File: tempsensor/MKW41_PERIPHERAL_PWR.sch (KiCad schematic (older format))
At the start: 39 parts, among them J3 Conn_ARM_JTAG_SWD_10, J4 USB_B_Micro, Q1 BSS806N, Q2 BSS806N, SW3 ~RST, SW4 ~INT, U6 BQ24012

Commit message: Added footprints to tempsensor.
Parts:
- C16, C25, C26: footprint (none) -> Capacitor_SMD:C_0603_1608Metric
- C17, C18, C19, C20, C22, C23, C24, C27, C28, C29, C30, C31, C32: footprint (none) -> Capacitor_SMD:C_0402_1005Metric
- J3: footprint (none) -> Connector_PinHeader_1.27mm:PinHeader_2x05_P1.27mm_Vertical_SMD
- L3, L4: footprint (none) -> Inductor_SMD:L_0402_1005Metric
- SW3: footprint Button_Switch_THT:SW_PUSH_6mm_H5mm -> Button_Switch_SMD:SW_SPST_Panasonic_EVQPL_3PL_5PL_PT_A08
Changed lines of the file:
@@
 F 0 "SW3" V 2504 1498 50  0000 L CNN
 F 1 "~RST" V 2595 1498 50  0000 L CNN
-F 2 "Button_Switch_THT:SW_PUSH_6mm_H5mm" H 2550 1550 50  0001 C CNN
+F 2 "Button_Switch_SMD:SW_SPST_Panasonic_EVQPL_3PL_5PL_PT_A08" H 2550 1550 50  0001 C CNN
 F 3 "~" H 2550 1550 50  0001 C CNN
 	1    2550 1350
@@
 F 0 "J3" H 700 1950 50  0000 R CNN
 F 1 "Conn_ARM_JTAG_SWD_10" H 1950 1950 50  0000 R CNN
-F 2 "" H 1000 1400 50  0001 C CNN
+F 2 "Connector_PinHeader_1.27mm:PinHeader_2x05_P1.27mm_Vertical_SMD" H 1000 1400 50  0001 C CNN
 F 3 "http://infocenter.arm.com/help/topic/com.arm.doc.ddi0314h/DDI0314H_coresight_components_trm.pdf" V 650 150 50  0001 C CNN
 	1    1000 1400
@@
 F 0 "C22" H 3565 1646 50  0000 L CNN
 F 1 "10n" H 3565 1555 50  0000 L CNN
-F 2 "" H 3488 1450 50  0001 C CNN
+F 2 "Capacitor_SMD:C_0402_1005Metric" H 3488 1450 50  0001 C CNN
 F 3 "~" H 3450 1600 50  0001 C CNN
 	1    3450 1600
@@
 F 0 "C16" H 9065 1046 50  0000 L CNN
 F 1 "10u" H 9065 955 50  0000 L CNN
-F 2 "" H 8988 850 50  0001 C CNN
+F 2 "Capacitor_SMD:C_0603_1608Metric" H 8988 850 50  0001 C CNN
 F 3 "~" H 8950 1000 50  0001 C CNN
 	1    8950 1000
@@
 F 0 "C18" H 9965 1046 50  0000 L CNN
 F 1 "1u" H 9965 955 50  0000 L CNN
-F 2 "" H 9888 850 50  0001 C CNN
+F 2 "Capacitor_SMD:C_0402_1005Metric" H 9888 850 50  0001 C CNN
 F 3 "~" H 9850 1000 50  0001 C CNN
 	1    9850 1000
@@
 F 0 "C19" H 10365 1046 50  0000 L CNN
 F 1 "100n" H 10365 955 50  0000 L CNN
-F 2 "" H 10288 850 50  0001 C CNN
+F 2 "Capacitor_SMD:C_0402_1005Metric" H 10288 850 50  0001 C CNN
 F 3 "~" H 10250 1000 50  0001 C CNN
 	1    10250 1000
@@
 F 0 "C20" H 10865 1046 50  0000 L CNN
 F 1 "100n" H 10865 955 50  0000 L CNN
-F 2 "" H 10788 850 50  0001 C CNN
+F 2 "Capacitor_SMD:C_0402_1005Metric" H 10788 850 50  0001 C CNN
 F 3 "~" H 10750 1000 50  0001 C CNN
 	1    10750 1000
@@
 F 0 "L3" V 10740 1750 50  0000 C CNN
 F 1 "100n" V 10649 1750 50  0000 C CNN
-F 2 "" H 10550 1750 50  0001 C CNN
+F 2 "Inductor_SMD:L_0402_1005Metric" H 10550 1750 50  0001 C CNN
 F 3 "~" H 10550 1750 50  0001 C CNN
 	1    10550 1750
@@
 F 0 "C23" H 10865 1996 50  0000 L CNN
 F 1 "1u" H 10865 1905 50  0000 L CNN
-F 2 "" H 10788 1800 50  0001 C CNN
+F 2 "Capacitor_SMD:C_0402_1005Metric" H 10788 1800 50  0001 C CNN
 F 3 "~" H 10750 1950 50  0001 C CNN
 	1    10750 1950
@@
 F 0 "C24" H 10865 2846 50  0000 L CNN
 F 1 "100n" H 10865 2755 50  0000 L CNN
-F 2 "" H 10788 2650 50  0001 C CNN
+F 2 "Capacitor_SMD:C_0402_1005Metric" H 10788 2650 50  0001 C CNN
 F 3 "~" H 10750 2800 50  0001 C CNN
 	1    10750 2800
@@
 F 0 "C26" H 8915 3746 50  0000 L CNN
 F 1 "10u" H 8915 3655 50  0000 L CNN
-F 2 "" H 8838 3550 50  0001 C CNN
+F 2 "Capacitor_SMD:C_0603_1608Metric" H 8838 3550 50  0001 C CNN
 F 3 "~" H 8800 3700 50  0001 C CNN
 	1    8800 3700
@@
 F 0 "L4" V 9190 3500 50  0000 C CNN
 F 1 "100n" V 9099 3500 50  0000 C CNN
-F 2 "" H 9000 3500 50  0001 C CNN
+F 2 "Inductor_SMD:L_0402_1005Metric" H 9000 3500 50  0001 C CNN
 F 3 "~" H 9000 3500 50  0001 C CNN
 	1    9000 3500
@@
 F 0 "C27" H 9315 3746 50  0000 L CNN
 F 1 "1u" H 9315 3655 50  0000 L CNN
-F 2 "" H 9238 3550 50  0001 C CNN
+F 2 "Capacitor_SMD:C_0402_1005Metric" H 9238 3550 50  0001 C CNN
 F 3 "~" H 9200 3700 50  0001 C CNN
 	1    9200 3700
@@
 F 0 "C28" H 9665 3746 50  0000 L CNN
 F 1 "1u" H 9665 3655 50  0000 L CNN
-F 2 "" H 9588 3550 50  0001 C CNN
+F 2 "Capacitor_SMD:C_0402_1005Metric" H 9588 3550 50  0001 C CNN
 F 3 "~" H 9550 3700 50  0001 C CNN
 	1    9550 3700
@@
 F 0 "C29" H 10015 3746 50  0000 L CNN
 F 1 "100n" H 10015 3655 50  0000 L CNN
-F 2 "" H 9938 3550 50  0001 C CNN
+F 2 "Capacitor_SMD:C_0402_1005Metric" H 9938 3550 50  0001 C CNN
 F 3 "~" H 9900 3700 50  0001 C CNN
 	1    9900 3700
@@
 F 0 "C30" H 10465 3746 50  0000 L CNN
 F 1 "12p" H 10465 3655 50  0000 L CNN
-F 2 "" H 10388 3550 50  0001 C CNN
+F 2 "Capacitor_SMD:C_0402_1005Metric" H 10388 3550 50  0001 C CNN
 F 3 "~" H 10350 3700 50  0001 C CNN
 	1    10350 3700
@@
 F 0 "C31" H 10865 3746 50  0000 L CNN
 F 1 "12p" H 10865 3655 50  0000 L CNN
-F 2 "" H 10788 3550 50  0001 C CNN
+F 2 "Capacitor_SMD:C_0402_1005Metric" H 10788 3550 50  0001 C CNN
 F 3 "~" H 10750 3700 50  0001 C CNN
 	1    10750 3700
@@
 F 0 "C17" H 9515 1046 50  0000 L CNN
 F 1 "1u" H 9515 955 50  0000 L CNN
-F 2 "" H 9438 850 50  0001 C CNN
+F 2 "Capacitor_SMD:C_0402_1005Metric" H 9438 850 50  0001 C CNN
 F 3 "~" H 9400 1000 50  0001 C CNN
 	1    9400 1000
@@
 F 0 "C25" V 1148 3350 50  0000 C CNN
 F 1 "1u" V 1239 3350 50  0000 C CNN
-F 2 "" H 1438 3200 50  0001 C CNN
+F 2 "Capacitor_SMD:C_0603_1608Metric" H 1438 3200 50  0001 C CNN
 F 3 "~" H 1400 3350 50  0001 C CNN
 	1    1400 3350
@@
 F 0 "C32" V 5848 4850 50  0000 C CNN
 F 1 "100n" V 5939 4850 50  0000 C CNN
-F 2 "" H 6138 4700 50  0001 C CNN
+F 2 "Capacitor_SMD:C_0402_1005Metric" H 6138 4700 50  0001 C CNN
 F 3 "~" H 6100 4850 50  0001 C CNN
 	1    6100 4850

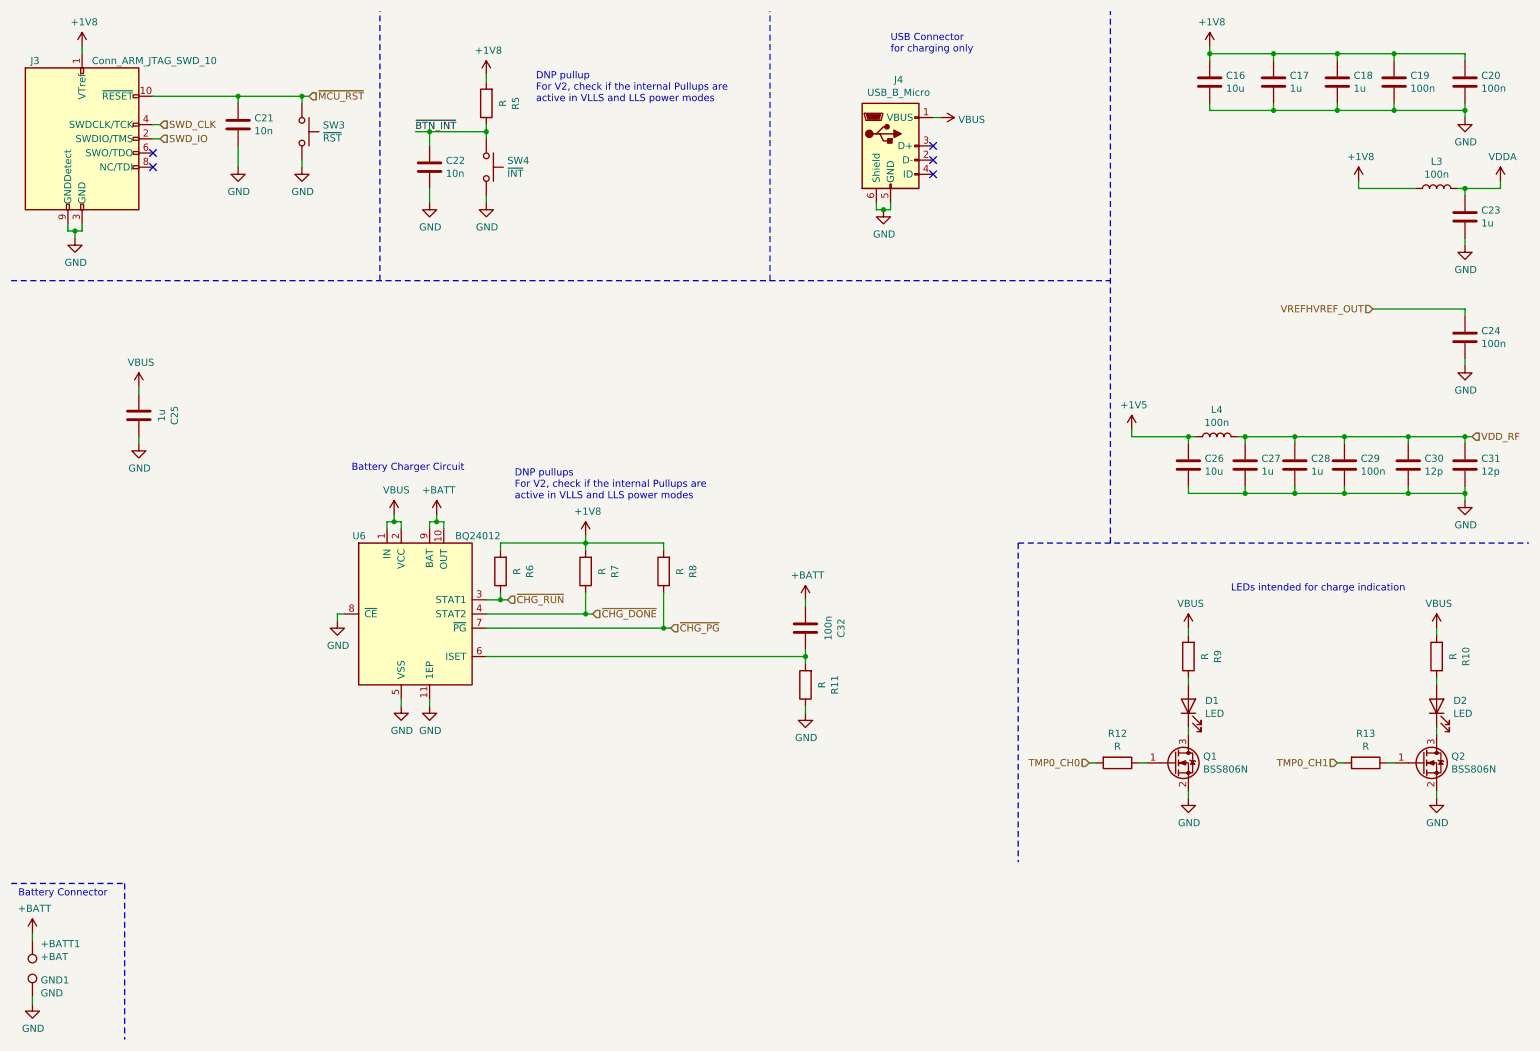
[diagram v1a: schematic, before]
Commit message: Started layouting the TempSensor, exchanged the large LEDs for 0603 LEDs (from ELAB). MCU needs to be placed. Changed signals on expansion header to put power pins onto just one end.
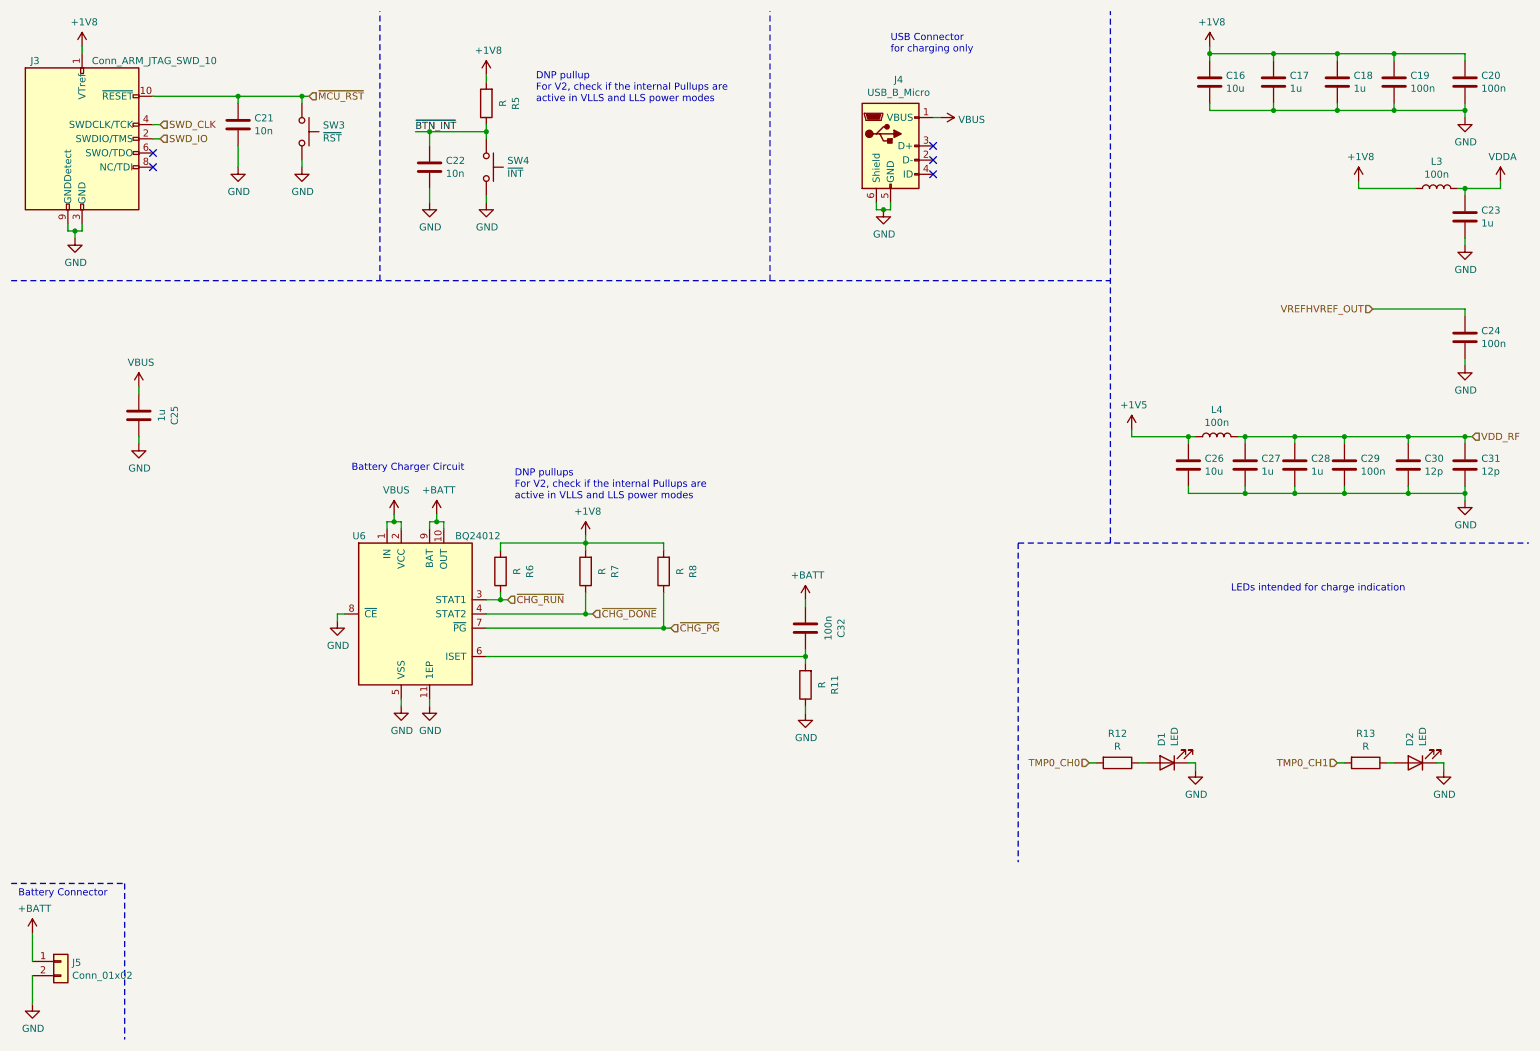
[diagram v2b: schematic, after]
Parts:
- removed +BATT1: +BAT, TestPoint:TestPoint_Pad_4.0x4.0mm, symbol Connector:TestPoint
- removed GND1: GND, TestPoint:TestPoint_Pad_4.0x4.0mm, symbol Connector:TestPoint
- removed Q1, Q2: BSS806N, Package_TO_SOT_SMD:SOT-23, symbol Device:Q_NMOS_GSD
- removed R10, R9: R, Resistor_SMD:R_0603_1608Metric, symbol Device:R
- added J5: Conn_01x02, Connector_PinHeader_2.54mm:PinHeader_1x02_P2.54mm_Vertical, symbol Connector_Generic:Conn_01x02
- D1, D2: footprint LED_SMD:LED_1210_3225Metric -> LED_SMD:LED_0603_1608Metric
- R11, R6, R7, R8: footprint Resistor_SMD:R_0603_1608Metric -> Resistor_SMD:R_0402_1005Metric
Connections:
- net +BATT: now also J5.1 (Pin_1)
- net GND: now also D1.1 (K), D2.1 (K), J5.2 (Pin_2)
- net at D1.2 (A): now also R12.1
- net at D2.2 (A): now also R13.1
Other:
- moved on the sheet: D1, D2
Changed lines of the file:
@@
 F 0 "R11" V 5893 5250 50  0000 C CNN
 F 1 "R" V 5984 5250 50  0000 C CNN
-F 2 "Resistor_SMD:R_0603_1608Metric" V 6030 5250 50  0001 C CNN
+F 2 "Resistor_SMD:R_0402_1005Metric" V 6030 5250 50  0001 C CNN
 F 3 "~" H 6100 5250 50  0001 C CNN
 	1    6100 5250
@@
 $EndComp
 $Comp
-L Connector:TestPoint GND?
-U 1 1 5FBA3E01
-P 650 7450
-AR Path="/5FBA3E01" Ref="GND?"  Part="1"
-AR Path="/5FB5B55F/5FBA3E01" Ref="GND1"  Part="1"
-F 0 "GND1" H 708 7568 50  0000 L CNN
-F 1 "GND" H 708 7477 50  0000 L CNN
-F 2 "TestPoint:TestPoint_Pad_4.0x4.0mm" H 850 7450 50  0001 C CNN
-F 3 "~" H 850 7450 50  0001 C CNN
-	1    650  7450
-	1    0    0    -1
-$EndComp
-$Comp
 L power:+BATT #PWR?
 U 1 1 5FBA3E07
@@
 	1    0    0    -1
 $EndComp
-Wire Wire Line
-	650  7000 650  7050
 $Comp
 L power:GND #PWR?
@@
 	1    0    0    -1
 $EndComp
-Wire Wire Line
-	650  7500 650  7450
 Text Notes 550  6750 0    50   ~ 0
 Battery Connector
@@
 Text Notes 2900 3750 0    50   ~ 0
 Battery Charger Circuit
-$Comp
-L Connector:TestPoint +BATT?
-U 1 1 5FBA3E1A
-P 650 7050
-AR Path="/5FBA3E1A" Ref="+BATT?"  Part="1"
-AR Path="/5FB5B55F/5FBA3E1A" Ref="+BATT1"  Part="1"
-F 0 "+BATT1" H 592 7076 50  0000 R CNN
-F 1 "+BAT" H 592 7167 50  0000 R CNN
-F 2 "TestPoint:TestPoint_Pad_4.0x4.0mm" H 850 7050 50  0001 C CNN
-F 3 "~" H 850 7050 50  0001 C CNN
-	1    650  7050
-	-1   0    0    1
-$EndComp
 $Comp
 L Connector:USB_B_Micro J?
@@
 L Device:LED D?
 U 1 1 5FBB870F
-P 8800 5400
+P 8650 5800
 AR Path="/5FBB870F" Ref="D?"  Part="1"
 AR Path="/5FB5B55F/5FBB870F" Ref="D1"  Part="1"
-F 0 "D1" V 8839 5282 50  0000 R CNN
-F 1 "LED" V 8748 5282 50  0000 R CNN
-F 2 "LED_SMD:LED_1210_3225Metric" H 8800 5400 50  0001 C CNN
-F 3 "~" H 8800 5400 50  0001 C CNN
-	1    8800 5400
-	0    -1   -1   0
-$EndComp
-$Comp
-L Device:Q_NMOS_GSD Q?
-U 1 1 5FBB8715
-P 8700 5800
-AR Path="/5FBB8715" Ref="Q?"  Part="1"
-AR Path="/5FB5B55F/5FBB8715" Ref="Q1"  Part="1"
-F 0 "Q1" H 8904 5846 50  0000 L CNN
-F 1 "BSS806N" H 8904 5755 50  0000 L CNN
-F 2 "Package_TO_SOT_SMD:SOT-23" H 8900 5900 50  0001 C CNN
-F 3 "~" H 8700 5800 50  0001 C CNN
-	1    8700 5800
-	1    0    0    -1
+F 0 "D1" V 8689 5682 50  0000 R CNN
+F 1 "LED" V 8598 5682 50  0000 R CNN
+F 2 "LED_SMD:LED_0603_1608Metric" H 8650 5800 50  0001 C CNN
+F 3 "~" H 8650 5800 50  0001 C CNN
+	1    8650 5800
+	-1   0    0    1
 $EndComp
 $Comp
@@
 L power:GND #PWR?
 U 1 1 5FBB8722
-P 8800 6050
+P 8850 5850
 AR Path="/5FBB8722" Ref="#PWR?"  Part="1"
 AR Path="/5FB5B55F/5FBB8722" Ref="#PWR071"  Part="1"
-F 0 "#PWR071" H 8800 5800 50  0001 C CNN
-F 1 "GND" H 8805 5877 50  0000 C CNN
-F 2 "" H 8800 6050 50  0001 C CNN
-F 3 "" H 8800 6050 50  0001 C CNN
-	1    8800 6050
-	1    0    0    -1
-$EndComp
-Wire Wire Line
-	8800 6050 8800 6000
-Wire Wire Line
-	8800 5550 8800 5600
-$Comp
-L Device:R R?
-U 1 1 5FBB872A
-P 8800 5050
-AR Path="/5FBB872A" Ref="R?"  Part="1"
-AR Path="/5FB5B55F/5FBB872A" Ref="R9"  Part="1"
-F 0 "R9" V 8593 5050 50  0000 C CNN
-F 1 "R" V 8684 5050 50  0000 C CNN
-F 2 "Resistor_SMD:R_0603_1608Metric" V 8730 5050 50  0001 C CNN
-F 3 "~" H 8800 5050 50  0001 C CNN
-	1    8800 5050
-	-1   0    0    1
-$EndComp
-Wire Wire Line
-	8800 5200 8800 5250
-Wire Wire Line
-	8800 4850 8800 4900
+F 0 "#PWR071" H 8850 5600 50  0001 C CNN
+F 1 "GND" H 8855 5677 50  0000 C CNN
+F 2 "" H 8850 5850 50  0001 C CNN
+F 3 "" H 8850 5850 50  0001 C CNN
+	1    8850 5850
+	1    0    0    -1
+$EndComp
 $Comp
 L Device:LED D?
 U 1 1 5FBB8738
-P 10550 5400
+P 10400 5800
 AR Path="/5FBB8738" Ref="D?"  Part="1"
 AR Path="/5FB5B55F/5FBB8738" Ref="D2"  Part="1"
-F 0 "D2" V 10589 5282 50  0000 R CNN
-F 1 "LED" V 10498 5282 50  0000 R CNN
-F 2 "LED_SMD:LED_1210_3225Metric" H 10550 5400 50  0001 C CNN
-F 3 "~" H 10550 5400 50  0001 C CNN
-	1    10550 5400
-	0    -1   -1   0
-$EndComp
-$Comp
-L Device:Q_NMOS_GSD Q?
-U 1 1 5FBB873E
-P 10450 5800
-AR Path="/5FBB873E" Ref="Q?"  Part="1"
-AR Path="/5FB5B55F/5FBB873E" Ref="Q2"  Part="1"
-F 0 "Q2" H 10654 5846 50  0000 L CNN
-F 1 "BSS806N" H 10654 5755 50  0000 L CNN
-F 2 "Package_TO_SOT_SMD:SOT-23" H 10650 5900 50  0001 C CNN
-F 3 "~" H 10450 5800 50  0001 C CNN
-	1    10450 5800
-	1    0    0    -1
+F 0 "D2" V 10439 5682 50  0000 R CNN
+F 1 "LED" V 10348 5682 50  0000 R CNN
+F 2 "LED_SMD:LED_0603_1608Metric" H 10400 5800 50  0001 C CNN
+F 3 "~" H 10400 5800 50  0001 C CNN
+	1    10400 5800
+	-1   0    0    1
 $EndComp
 $Comp
@@
 L power:GND #PWR?
 U 1 1 5FBB874B
-P 10550 6050
+P 10600 5850
 AR Path="/5FBB874B" Ref="#PWR?"  Part="1"
 AR Path="/5FB5B55F/5FBB874B" Ref="#PWR072"  Part="1"
-F 0 "#PWR072" H 10550 5800 50  0001 C CNN
-F 1 "GND" H 10555 5877 50  0000 C CNN
-F 2 "" H 10550 6050 50  0001 C CNN
-F 3 "" H 10550 6050 50  0001 C CNN
-	1    10550 6050
-	1    0    0    -1
-$EndComp
-Wire Wire Line
-	10550 6050 10550 6000
-Wire Wire Line
-	10550 5550 10550 5600
-$Comp
-L Device:R R?
-U 1 1 5FBB8753
-P 10550 5050
-AR Path="/5FBB8753" Ref="R?"  Part="1"
-AR Path="/5FB5B55F/5FBB8753" Ref="R10"  Part="1"
-F 0 "R10" V 10343 5050 50  0000 C CNN
-F 1 "R" V 10434 5050 50  0000 C CNN
-F 2 "Resistor_SMD:R_0603_1608Metric" V 10480 5050 50  0001 C CNN
-F 3 "~" H 10550 5050 50  0001 C CNN
-	1    10550 5050
-	-1   0    0    1
-$EndComp
-Wire Wire Line
-	10550 5200 10550 5250
-Wire Wire Line
-	10550 4850 10550 4900
+F 0 "#PWR072" H 10600 5600 50  0001 C CNN
+F 1 "GND" H 10605 5677 50  0000 C CNN
+F 2 "" H 10600 5850 50  0001 C CNN
+F 3 "" H 10600 5850 50  0001 C CNN
+	1    10600 5850
+	1    0    0    -1
+$EndComp
 Wire Wire Line
 	8100 5800 8150 5800
@@
 Text Notes 9100 4600 0    50   ~ 0
 LEDs intended for charge indication
-$Comp
-L power:VBUS #PWR?
-U 1 1 5FC21E54
-P 8800 4850
-AR Path="/5FC21E54" Ref="#PWR?"  Part="1"
-AR Path="/5FB5B55F/5FC21E54" Ref="#PWR066"  Part="1"
-F 0 "#PWR066" H 8800 4700 50  0001 C CNN
-F 1 "VBUS" H 8815 5023 50  0000 C CNN
-F 2 "" H 8800 4850 50  0001 C CNN
-F 3 "" H 8800 4850 50  0001 C CNN
-	1    8800 4850
-	1    0    0    -1
-$EndComp
-$Comp
-L power:VBUS #PWR?
-U 1 1 5FC23977
-P 10550 4850
-AR Path="/5FC23977" Ref="#PWR?"  Part="1"
-AR Path="/5FB5B55F/5FC23977" Ref="#PWR067"  Part="1"
-F 0 "#PWR067" H 10550 4700 50  0001 C CNN
-F 1 "VBUS" H 10565 5023 50  0000 C CNN
-F 2 "" H 10550 4850 50  0001 C CNN
-F 3 "" H 10550 4850 50  0001 C CNN
-	1    10550 4850
-	1    0    0    -1
-$EndComp
 Text HLabel 10100 2600 0    50   Input ~ 0
 VREFHVREF_OUT
@@
 F 0 "R8" V 4893 4450 50  0000 C CNN
 F 1 "R" V 4984 4450 50  0000 C CNN
-F 2 "Resistor_SMD:R_0603_1608Metric" V 5030 4450 50  0001 C CNN
+F 2 "Resistor_SMD:R_0402_1005Metric" V 5030 4450 50  0001 C CNN
 F 3 "~" H 5100 4450 50  0001 C CNN
 	1    5100 4450
@@
 F 0 "R7" V 4343 4450 50  0000 C CNN
 F 1 "R" V 4434 4450 50  0000 C CNN
-F 2 "Resistor_SMD:R_0603_1608Metric" V 4480 4450 50  0001 C CNN
+F 2 "Resistor_SMD:R_0402_1005Metric" V 4480 4450 50  0001 C CNN
 F 3 "~" H 4550 4450 50  0001 C CNN
 	1    4550 4450
@@
 F 0 "R6" V 3743 4450 50  0000 C CNN
 F 1 "R" V 3834 4450 50  0000 C CNN
-F 2 "Resistor_SMD:R_0603_1608Metric" V 3880 4450 50  0001 C CNN
+F 2 "Resistor_SMD:R_0402_1005Metric" V 3880 4450 50  0001 C CNN
 F 3 "~" H 3950 4450 50  0001 C CNN
 	1    3950 4450
@@
 Wire Wire Line
 	3850 5050 6100 5050
+Wire Wire Line
+	10600 5850 10600 5800
+Wire Wire Line
+	10600 5800 10550 5800
+Wire Wire Line
+	8850 5850 8850 5800
+Wire Wire Line
+	8850 5800 8800 5800
+$Comp
+L Connector_Generic:Conn_01x02 J5
+U 1 1 5FC07FE0
+P 850 7200
+F 0 "J5" H 930 7192 50  0000 L CNN
+F 1 "Conn_01x02" H 930 7101 50  0000 L CNN
+F 2 "Connector_PinHeader_2.54mm:PinHeader_1x02_P2.54mm_Vertical" H 850 7200 50  0001 C CNN
+F 3 "~" H 850 7200 50  0001 C CNN
+	1    850  7200
+	1    0    0    -1
+$EndComp
+Wire Wire Line
+	650  7000 650  7200
+Wire Wire Line
+	650  7300 650  7500
 $EndSCHEMATC
